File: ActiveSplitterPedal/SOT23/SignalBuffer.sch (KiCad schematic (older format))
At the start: 4 parts, among them U1 OPA842, U5 DG468DV_T1_E3

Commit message: updated schematic
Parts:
- added R15: 2K2, Resistor_SMD:R_0805_2012Metric_Pad1.15x1.40mm_HandSolder, symbol Device:R
- added R19, R20: 100R, Resistor_SMD:R_0805_2012Metric_Pad1.15x1.40mm_HandSolder, symbol Device:R
- added RV1: 5K, Potentiometer_THT:Potentiometer_Alps_RK09L_Single_Vertical, symbol Device:R_POT
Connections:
- net GNDS: now also U1.3 (+)
- net IN: now also R15.2; no longer U1.3 (+)
- net at U1.1, U5.1 (NO): now also R20.1; no longer U1.4 (-)
- new net: R15.1, R19.2, U1.4 (-)
- new net: R19.1, RV1.1, RV1.2
- new net: R20.2, RV1.3
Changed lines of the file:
@@
 $EndDescr
 Wire Wire Line
-	2600 3000 3250 3000
-Wire Wire Line
-	3250 3200 3075 3200
-Wire Wire Line
-	3075 3200 3075 4450
-Wire Wire Line
-	3075 4450 4050 4450
-Wire Wire Line
-	4050 4450 4050 3100
-Wire Wire Line
-	4050 3100 3850 3100
-Wire Wire Line
-	4050 3100 6550 3100
-Connection ~ 4050 3100
+	1900 3650 2200 3650
 Wire Wire Line
 	6550 3350 6100 3350
@@
 Text HLabel 6100 3350 0    50   Input ~ 0
 SW
-Text HLabel 2600 3000 0    50   Input ~ 0
+Text HLabel 1900 3650 0    50   Input ~ 0
 IN
 Text HLabel 7850 3100 2    50   Input ~ 0
 OUT
 $Comp
-L Amplifier_Operational:OPA842xDBV U1
-U 1 1 5F35E576
-P 3550 3100
-AR Path="/5F350192/5F35E576" Ref="U1"  Part="1"
-AR Path="/5F3658F9/5F35E576" Ref="U2"  Part="1"
-AR Path="/5F365961/5F35E576" Ref="U3"  Part="1"
-AR Path="/5F365B82/5F35E576" Ref="U4"  Part="1"
-F 0 "U1" H 3550 3650 50  0000 L CNN
-F 1 "OPA842" H 3500 3450 50  0000 L CNN
-F 2 "Package_TO_SOT_SMD:SOT-23-5" H 3450 2900 50  0001 L CNN
-F 3 "http://www.ti.com/lit/ds/symlink/opa842.pdf" H 3550 3300 50  0001 C CNN
-	1    3550 3100
-	1    0    0    -1
-$EndComp
-Wire Wire Line
-	3450 3400 3450 3800
-$Comp
-L power:-5V #PWR017
-U 1 1 5F361BF5
-P 3450 3800
-AR Path="/5F350192/5F361BF5" Ref="#PWR017"  Part="1"
-AR Path="/5F3658F9/5F361BF5" Ref="#PWR019"  Part="1"
-AR Path="/5F365961/5F361BF5" Ref="#PWR021"  Part="1"
-AR Path="/5F365B82/5F361BF5" Ref="#PWR023"  Part="1"
-F 0 "#PWR017" H 3450 3900 50  0001 C CNN
-F 1 "-5V" H 3465 3973 50  0000 C CNN
-F 2 "" H 3450 3800 50  0001 C CNN
-F 3 "" H 3450 3800 50  0001 C CNN
-	1    3450 3800
-	-1   0    0    1
-$EndComp
-$Comp
 L power:+5V #PWR016
 U 1 1 5F361F40
-P 3450 2250
+P 3450 2400
 AR Path="/5F350192/5F361F40" Ref="#PWR016"  Part="1"
 AR Path="/5F3658F9/5F361F40" Ref="#PWR018"  Part="1"
 AR Path="/5F365961/5F361F40" Ref="#PWR020"  Part="1"
 AR Path="/5F365B82/5F361F40" Ref="#PWR022"  Part="1"
-F 0 "#PWR016" H 3450 2100 50  0001 C CNN
-F 1 "+5V" H 3465 2423 50  0000 C CNN
-F 2 "" H 3450 2250 50  0001 C CNN
-F 3 "" H 3450 2250 50  0001 C CNN
-	1    3450 2250
-	1    0    0    -1
-$EndComp
-Wire Wire Line
-	3450 2250 3450 2800
+F 0 "#PWR016" H 3450 2250 50  0001 C CNN
+F 1 "+5V" H 3600 2450 50  0000 C CNN
+F 2 "" H 3450 2400 50  0001 C CNN
+F 3 "" H 3450 2400 50  0001 C CNN
+	1    3450 2400
+	1    0    0    -1
+$EndComp
+Wire Wire Line
+	3450 2400 3450 2800
 $Comp
 L power:+5V #PWR0101
@@
 	1    0    0    -1
 $EndComp
+$Comp
+L power:-5V #PWR017
+U 1 1 5F361BF5
+P 3450 3600
+AR Path="/5F350192/5F361BF5" Ref="#PWR017"  Part="1"
+AR Path="/5F3658F9/5F361BF5" Ref="#PWR019"  Part="1"
+AR Path="/5F365961/5F361BF5" Ref="#PWR021"  Part="1"
+AR Path="/5F365B82/5F361BF5" Ref="#PWR023"  Part="1"
+F 0 "#PWR017" H 3450 3700 50  0001 C CNN
+F 1 "-5V" H 3300 3650 50  0000 C CNN
+F 2 "" H 3450 3600 50  0001 C CNN
+F 3 "" H 3450 3600 50  0001 C CNN
+	1    3450 3600
+	-1   0    0    1
+$EndComp
+Wire Wire Line
+	3450 3400 3450 3600
+Wire Wire Line
+	4200 3100 6550 3100
+Wire Wire Line
+	4200 3100 3850 3100
+Connection ~ 4200 3100
+Wire Wire Line
+	4200 4050 4200 3100
+Wire Wire Line
+	3000 4050 3050 4050
+Wire Wire Line
+	3000 3200 3000 3650
+Wire Wire Line
+	3250 3200 3000 3200
+$Comp
+L Amplifier_Operational:OPA842xDBV U1
+U 1 1 5F35E576
+P 3550 3100
+AR Path="/5F350192/5F35E576" Ref="U1"  Part="1"
+AR Path="/5F3658F9/5F35E576" Ref="U2"  Part="1"
+AR Path="/5F365961/5F35E576" Ref="U3"  Part="1"
+AR Path="/5F365B82/5F35E576" Ref="U4"  Part="1"
+F 0 "U1" H 3100 3500 50  0000 L CNN
+F 1 "OPA842" H 3050 3400 50  0000 L CNN
+F 2 "Package_TO_SOT_SMD:SOT-23-5" H 3450 2900 50  0001 L CNN
+F 3 "http://www.ti.com/lit/ds/symlink/opa842.pdf" H 3550 3300 50  0001 C CNN
+	1    3550 3100
+	1    0    0    -1
+$EndComp
+$Comp
+L Device:R R15
+U 1 1 5F374B42
+P 2350 3650
+AR Path="/5F350192/5F374B42" Ref="R15"  Part="1"
+AR Path="/5F365B82/5F374B42" Ref="R9"  Part="1"
+AR Path="/5F365961/5F374B42" Ref="R11"  Part="1"
+AR Path="/5F3658F9/5F374B42" Ref="R13"  Part="1"
+F 0 "R15" V 2450 3650 50  0000 C CNN
+F 1 "2K2" V 2550 3650 50  0000 C CNN
+F 2 "Resistor_SMD:R_0805_2012Metric_Pad1.15x1.40mm_HandSolder" V 2280 3650 50  0001 C CNN
+F 3 "~" H 2350 3650 50  0001 C CNN
+	1    2350 3650
+	0    1    1    0
+$EndComp
+Wire Wire Line
+	2500 3650 3000 3650
+Wire Wire Line
+	3800 4050 3850 4050
+Connection ~ 3000 3650
+Wire Wire Line
+	3000 3650 3000 4050
+Wire Wire Line
+	3250 3000 2600 3000
+Wire Wire Line
+	2600 3000 2600 3200
+$Comp
+L power:GNDS #PWR047
+U 1 1 5F377EED
+P 2600 3200
+AR Path="/5F350192/5F377EED" Ref="#PWR047"  Part="1"
+AR Path="/5F365B82/5F377EED" Ref="#PWR044"  Part="1"
+AR Path="/5F365961/5F377EED" Ref="#PWR045"  Part="1"
+AR Path="/5F3658F9/5F377EED" Ref="#PWR046"  Part="1"
+F 0 "#PWR047" H 2600 2950 50  0001 C CNN
+F 1 "GNDS" H 2605 3027 50  0000 C CNN
+F 2 "" H 2600 3200 50  0001 C CNN
+F 3 "" H 2600 3200 50  0001 C CNN
+	1    2600 3200
+	1    0    0    -1
+$EndComp
+$Comp
+L Device:R_POT RV1
+U 1 1 5F37ADE4
+P 3650 4050
+AR Path="/5F350192/5F37ADE4" Ref="RV1"  Part="1"
+AR Path="/5F365B82/5F37ADE4" Ref="RV4"  Part="1"
+AR Path="/5F365961/5F37ADE4" Ref="RV3"  Part="1"
+AR Path="/5F3658F9/5F37ADE4" Ref="RV2"  Part="1"
+F 0 "RV1" V 4000 4150 50  0000 C CNN
+F 1 "5K" V 4100 4150 50  0000 C CNN
+F 2 "Potentiometer_THT:Potentiometer_Alps_RK09L_Single_Vertical" H 3650 4050 50  0001 C CNN
+F 3 "https://docs.rs-online.com/3ea0/0900766b80f4c570.pdf" H 3650 4050 50  0001 C CNN
+	1    3650 4050
+	0    -1   1    0
+$EndComp
+Wire Wire Line
+	3650 4200 3650 4300
+Wire Wire Line
+	3650 4300 3450 4300
+Wire Wire Line
+	3450 4300 3450 4050
+Connection ~ 3450 4050
+Wire Wire Line
+	3450 4050 3500 4050
+$Comp
+L Device:R R19
+U 1 1 5F37F653
+P 3200 4050
+AR Path="/5F350192/5F37F653" Ref="R19"  Part="1"
+AR Path="/5F365B82/5F37F653" Ref="R10"  Part="1"
+AR Path="/5F365961/5F37F653" Ref="R14"  Part="1"
+AR Path="/5F3658F9/5F37F653" Ref="R17"  Part="1"
+F 0 "R19" V 3300 4050 50  0000 C CNN
+F 1 "100R" V 3400 4050 50  0000 C CNN
+F 2 "Resistor_SMD:R_0805_2012Metric_Pad1.15x1.40mm_HandSolder" V 3130 4050 50  0001 C CNN
+F 3 "~" H 3200 4050 50  0001 C CNN
+	1    3200 4050
+	0    1    1    0
+$EndComp
+Wire Wire Line
+	3350 4050 3450 4050
+$Comp
+L Device:R R20
+U 1 1 5F37FC84
+P 4000 4050
+AR Path="/5F350192/5F37FC84" Ref="R20"  Part="1"
+AR Path="/5F365B82/5F37FC84" Ref="R12"  Part="1"
+AR Path="/5F365961/5F37FC84" Ref="R16"  Part="1"
+AR Path="/5F3658F9/5F37FC84" Ref="R18"  Part="1"
+F 0 "R20" V 4100 4050 50  0000 C CNN
+F 1 "100R" V 4200 4050 50  0000 C CNN
+F 2 "Resistor_SMD:R_0805_2012Metric_Pad1.15x1.40mm_HandSolder" V 3930 4050 50  0001 C CNN
+F 3 "~" H 4000 4050 50  0001 C CNN
+	1    4000 4050
+	0    1    1    0
+$EndComp
+Wire Wire Line
+	4150 4050 4200 4050
 $EndSCHEMATC

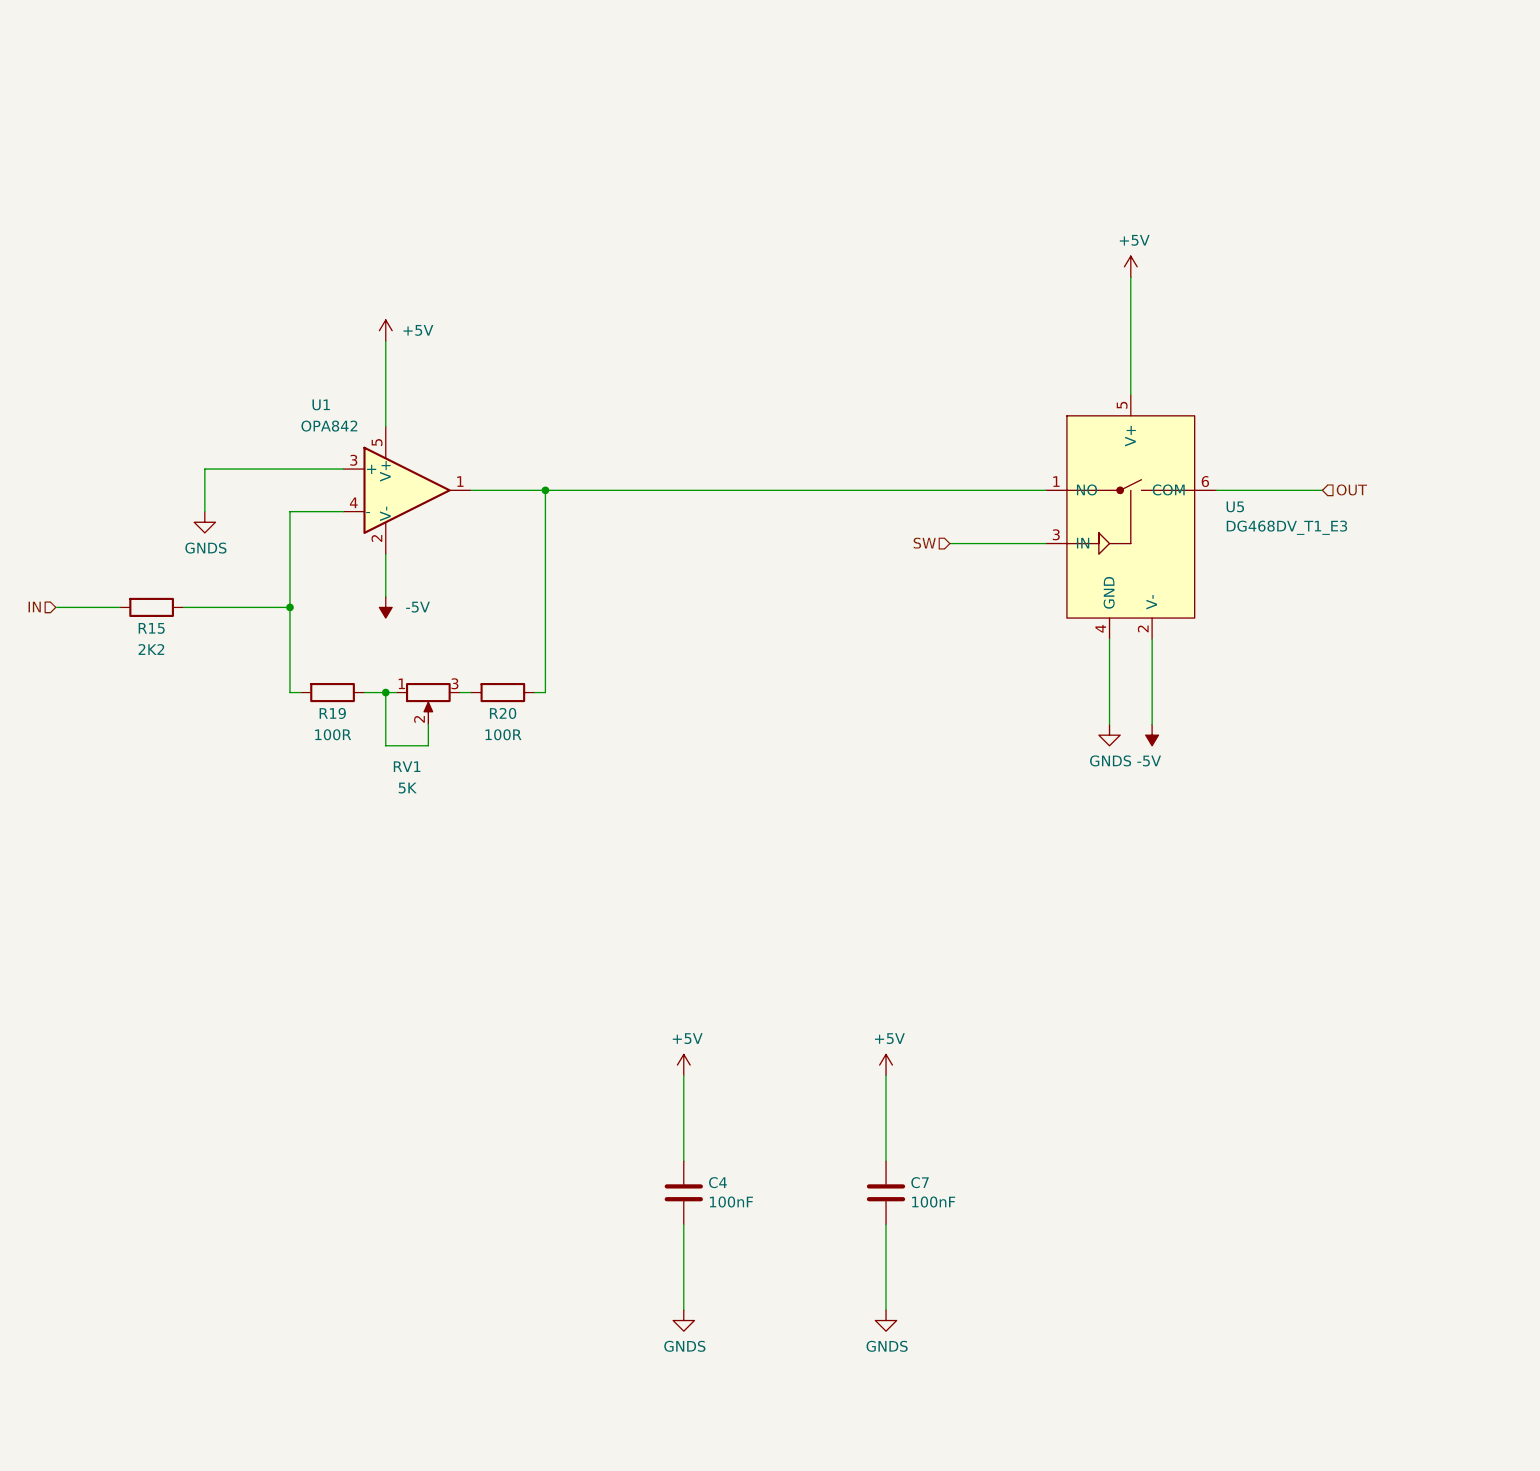
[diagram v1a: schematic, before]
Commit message: SOT23 REVA draft layout completed
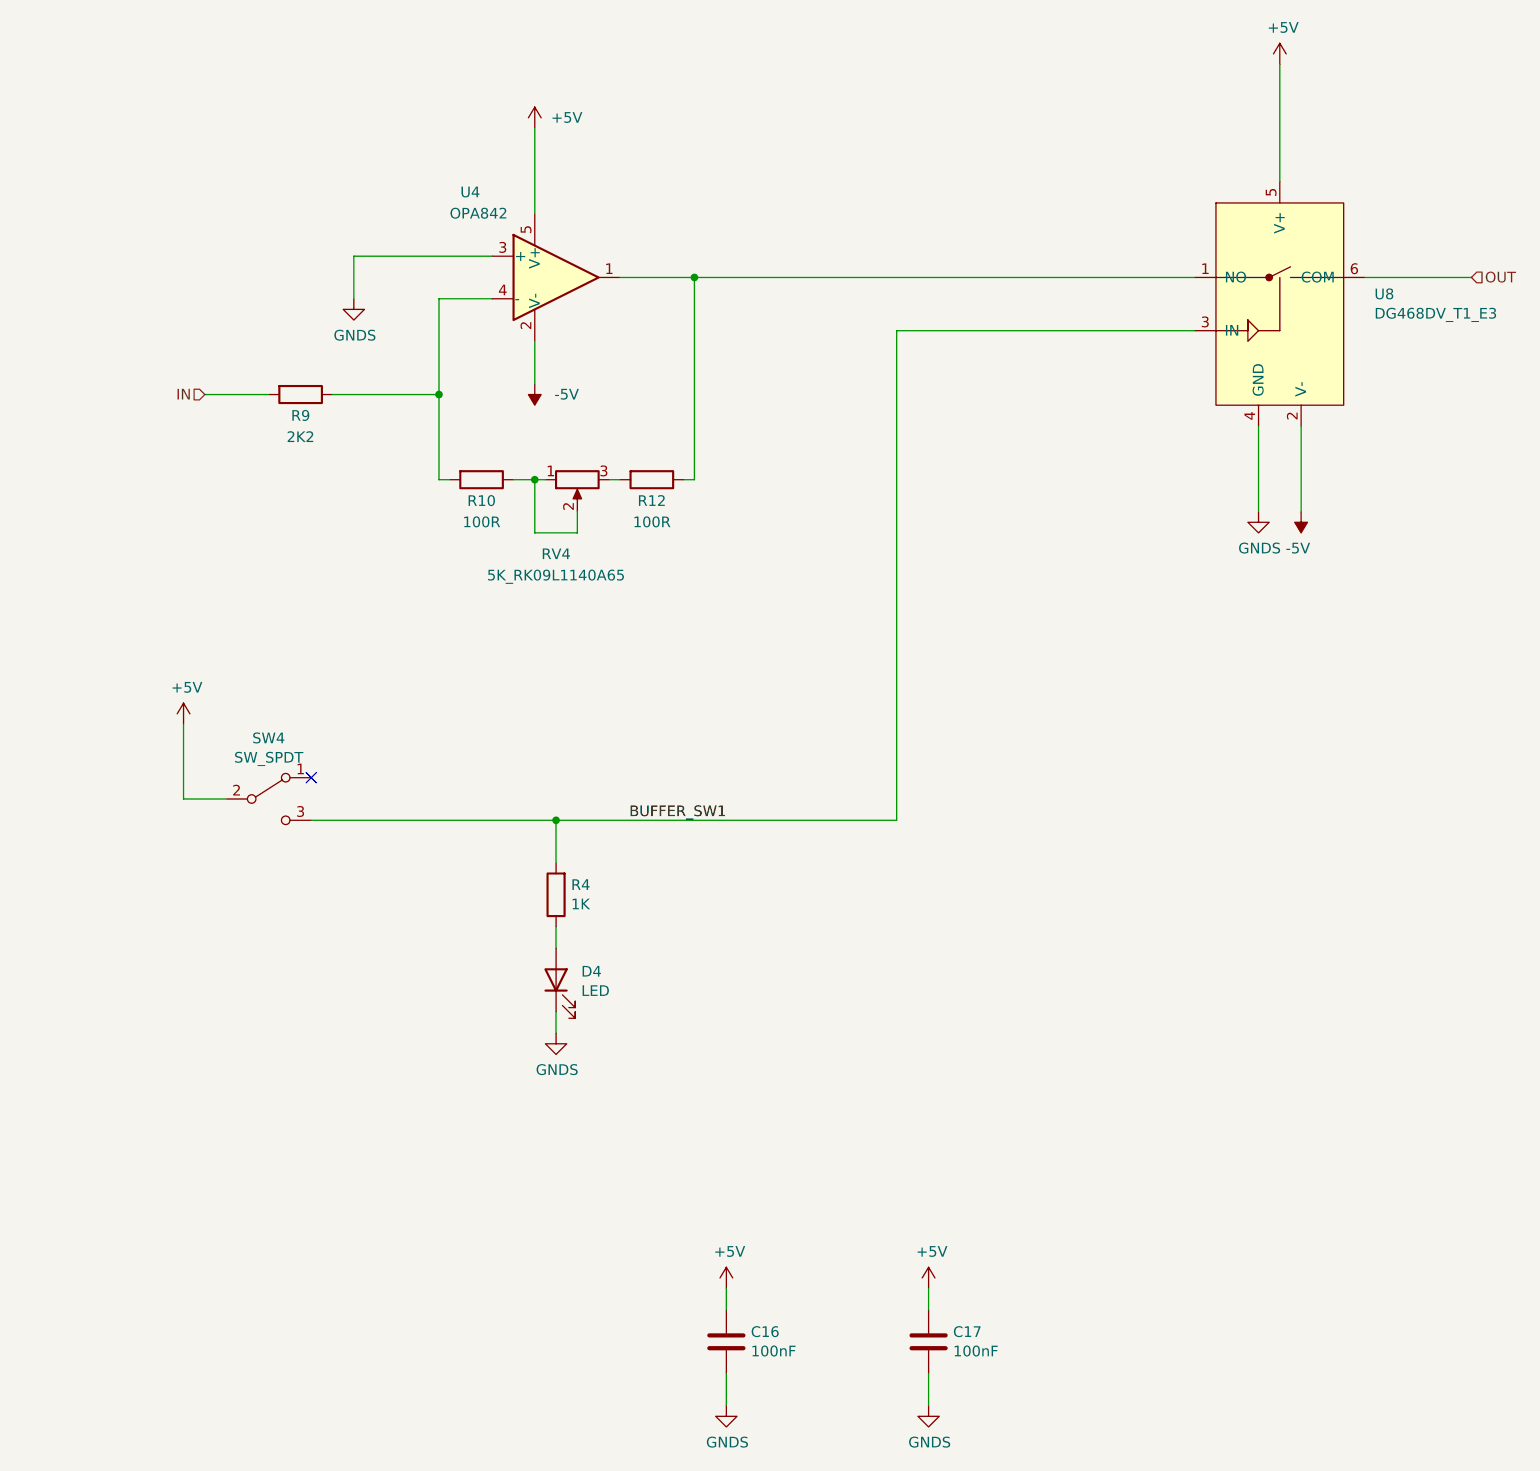
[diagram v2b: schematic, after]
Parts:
- added D1: LED, LED_THT:LED_D5.0mm, symbol Device:LED
- added R1: 1K, Resistor_SMD:R_0805_2012Metric_Pad1.15x1.40mm_HandSolder, symbol Device:R
- added SW1: SW_SPDT, RS_Switches:SPDT_Slide_Switch_Latching_Vertical_THT_8x9.3mm_734-7303, symbol Switch:SW_SPDT
- RV1: value 5K -> 5K_RK09L1140A65
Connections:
- net +5V: now also SW1.2 (B)
- net GNDS: now also D1.1 (K)
- net SW renamed BUFFER_SW1
- net BUFFER_SW1: now also R1.2, SW1.3 (C)
- new net: D1.2 (A), R1.1
- no-connect marks 0 -> 1
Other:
- moved on the sheet: C16, C17, R10, R12, R9, RV4, U4, U8
